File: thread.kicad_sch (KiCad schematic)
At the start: 35 parts, among them J3002 TC2050, J3003 Conn_01x06_Pin, J3004 SMA-KWE901, Q3001 DMG1012T, U3001 nRF52840, X3001 32.768kHz, X3002 25MHz

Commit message: Small fixes
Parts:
- added R3005: 10k, symbol Device:R
- R3003: value 100k -> 10k
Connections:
- net VDD_nRF: now also R3005.1
- net nRF_SPI0_CS0: now also R3005.2
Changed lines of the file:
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@@
 	)
 	(junction
+		(at 217.17 142.24)
+		(diameter 0)
+		(color 0 0 0 0)
+	)
+	(junction
 		(at 80.01 153.67)
 		(diameter 0)
@@
 	(wire
 		(pts
-			(xy 193.04 147.32) (xy 210.82 147.32)
-		)
-		(stroke
-			(width 0)
-			(type default)
-		)
-	)
-	(wire
-		(pts
 			(xy 316.23 113.03) (xy 316.23 115.57)
 		)
@@
 	(wire
 		(pts
+			(xy 204.47 149.86) (xy 222.25 149.86)
+		)
+		(stroke
+			(width 0)
+			(type default)
+		)
+	)
+	(wire
+		(pts
 			(xy 283.21 119.38) (xy 283.21 120.65)
 		)
@@
 	(wire
 		(pts
+			(xy 217.17 140.97) (xy 217.17 142.24)
+		)
+		(stroke
+			(width 0)
+			(type default)
+		)
+	)
+	(wire
+		(pts
 			(xy 69.85 161.29) (xy 69.85 163.83)
 		)
@@
 	(wire
 		(pts
+			(xy 217.17 132.08) (xy 217.17 133.35)
+		)
+		(stroke
+			(width 0)
+			(type default)
+		)
+	)
+	(wire
+		(pts
 			(xy 201.93 74.93) (xy 201.93 77.47)
 		)
@@
 	(wire
 		(pts
+			(xy 193.04 147.32) (xy 222.25 147.32)
+		)
+		(stroke
+			(width 0)
+			(type default)
+		)
+	)
+	(wire
+		(pts
 			(xy 229.87 220.98) (xy 250.19 220.98)
 		)
@@
 	(wire
 		(pts
-			(xy 193.04 142.24) (xy 210.82 142.24)
+			(xy 193.04 142.24) (xy 217.17 142.24)
 		)
 		(stroke
@@
 	(wire
 		(pts
+			(xy 217.17 142.24) (xy 222.25 142.24)
+		)
+		(stroke
+			(width 0)
+			(type default)
+		)
+	)
+	(wire
+		(pts
 			(xy 229.87 218.44) (xy 250.19 218.44)
 		)
@@
 	(wire
 		(pts
-			(xy 193.04 144.78) (xy 210.82 144.78)
-		)
-		(stroke
-			(width 0)
-			(type default)
-		)
-	)
-	(wire
-		(pts
 			(xy 64.77 219.71) (xy 73.66 219.71)
 		)
@@
 	(wire
 		(pts
-			(xy 193.04 132.08) (xy 213.36 132.08)
+			(xy 193.04 144.78) (xy 222.25 144.78)
 		)
 		(stroke
@@
 	(wire
 		(pts
-			(xy 210.82 149.86) (xy 204.47 149.86)
+			(xy 193.04 132.08) (xy 213.36 132.08)
 		)
 		(stroke
@@
 	(global_label "nRF_SPI0_CLK"
 		(shape input)
-		(at 210.82 144.78 0)
+		(at 222.25 144.78 0)
 		(fields_autoplaced yes)
 		(effects
@@
 		)
 		(property "Intersheetrefs" "${INTERSHEET_REFS}"
-			(at 227.1099 144.78 0)
+			(at 238.5399 144.78 0)
 			(effects
 				(font
@@
 	(global_label "nRF_SPI0_MOSI"
 		(shape input)
-		(at 210.82 147.32 0)
+		(at 222.25 147.32 0)
 		(fields_autoplaced yes)
 		(effects
@@
 		)
 		(property "Intersheetrefs" "${INTERSHEET_REFS}"
-			(at 228.138 147.32 0)
+			(at 239.568 147.32 0)
 			(effects
 				(font
@@
 	(global_label "nRF_SPI0_CS0"
 		(shape input)
-		(at 210.82 142.24 0)
+		(at 222.25 142.24 0)
 		(fields_autoplaced yes)
 		(effects
@@
 		)
 		(property "Intersheetrefs" "${INTERSHEET_REFS}"
-			(at 227.2308 142.24 0)
+			(at 238.6608 142.24 0)
 			(effects
 				(font
@@
 	(global_label "nRF_SPI0_MISO"
 		(shape input)
-		(at 210.82 149.86 0)
+		(at 222.25 149.86 0)
 		(fields_autoplaced yes)
 		(effects
@@
 		)
 		(property "Intersheetrefs" "${INTERSHEET_REFS}"
-			(at 228.138 149.86 0)
+			(at 239.568 149.86 0)
 			(effects
 				(font
@@
 			)
 		)
-		(property "Value" "100k"
+		(property "Value" "10k"
 			(at 208.28 191.7699 0)
 			(effects
@@
 	)
 	(symbol
+		(lib_id "Device:R")
+		(at 217.17 137.16 0)
+		(unit 1)
+		(exclude_from_sim no)
+		(in_bom yes)
+		(on_board yes)
+		(dnp no)
+		(property "Reference" "R3005"
+			(at 218.948 133.858 0)
+			(effects
+				(font
+					(size 1.27 1.27)
+				)
+				(justify left)
+			)
+		)
+		(property "Value" "10k"
+			(at 218.948 136.398 0)
+			(effects
+				(font
+					(size 1.27 1.27)
+				)
+				(justify left)
+			)
+		)
+		(property "Footprint" ""
+			(at 215.392 137.16 90)
+			(effects
+				(font
+					(size 1.27 1.27)
+				)
+				(hide yes)
+			)
+		)
+		(property "Datasheet" "~"
+			(at 217.17 137.16 0)
+			(effects
+				(font
+					(size 1.27 1.27)
+				)
+				(hide yes)
+			)
+		)
+		(property "Description" "Resistor"
+			(at 217.17 137.16 0)
+			(effects
+				(font
+					(size 1.27 1.27)
+				)
+				(hide yes)
+			)
+		)
+		(pin "2"
+		)
+		(pin "1"
+		)
+		(instances
+			(project ""
+				(path "/b43b7bca-e50d-42ec-8ff0-e0016dfefe0a/ab846a80-6f2e-4d25-9090-1f6af1d6fbdd"
+					(reference "R3005")
+					(unit 1)
+				)
+			)
+		)
+	)
+	(symbol
 		(lib_id "power:GND")
 		(at 226.06 135.89 0)
@@
 					(unit 1)
 				)
+			)
+		)
+	)
+	(symbol
+		(lib_id "power:VDD")
+		(at 217.17 132.08 0)
+		(unit 1)
+		(exclude_from_sim no)
+		(in_bom yes)
+		(on_board yes)
+		(dnp no)
+		(property "Reference" "#PWR03030"
+			(at 217.17 135.89 0)
+			(effects
+				(font
+					(size 1.27 1.27)
+				)
+				(hide yes)
+			)
+		)
+		(property "Value" "VDD_nRF"
+			(at 219.202 127.762 0)
+			(effects
+				(font
+					(size 1.27 1.27)
+				)
+			)
+		)
+		(property "Footprint" ""
+			(at 217.17 132.08 0)
+			(effects
+				(font
+					(size 1.27 1.27)
+				)
+				(hide yes)
+			)
+		)
+		(property "Datasheet" ""
+			(at 217.17 132.08 0)
+			(effects
+				(font
+					(size 1.27 1.27)
+				)
+				(hide yes)
+			)
+		)
+		(property "Description" "Power symbol creates a global label with name \"VDD\""
+			(at 217.17 132.08 0)
+			(effects
+				(font
+					(size 1.27 1.27)
+				)
+				(hide yes)
+			)
+		)
+		(pin "1"
+		)
+		(instances
+			(project "Leonhart"
+				(path "/b43b7bca-e50d-42ec-8ff0-e0016dfefe0a/ab846a80-6f2e-4d25-9090-1f6af1d6fbdd"
+					(reference "#PWR03030")
+					(unit 1)
+				)

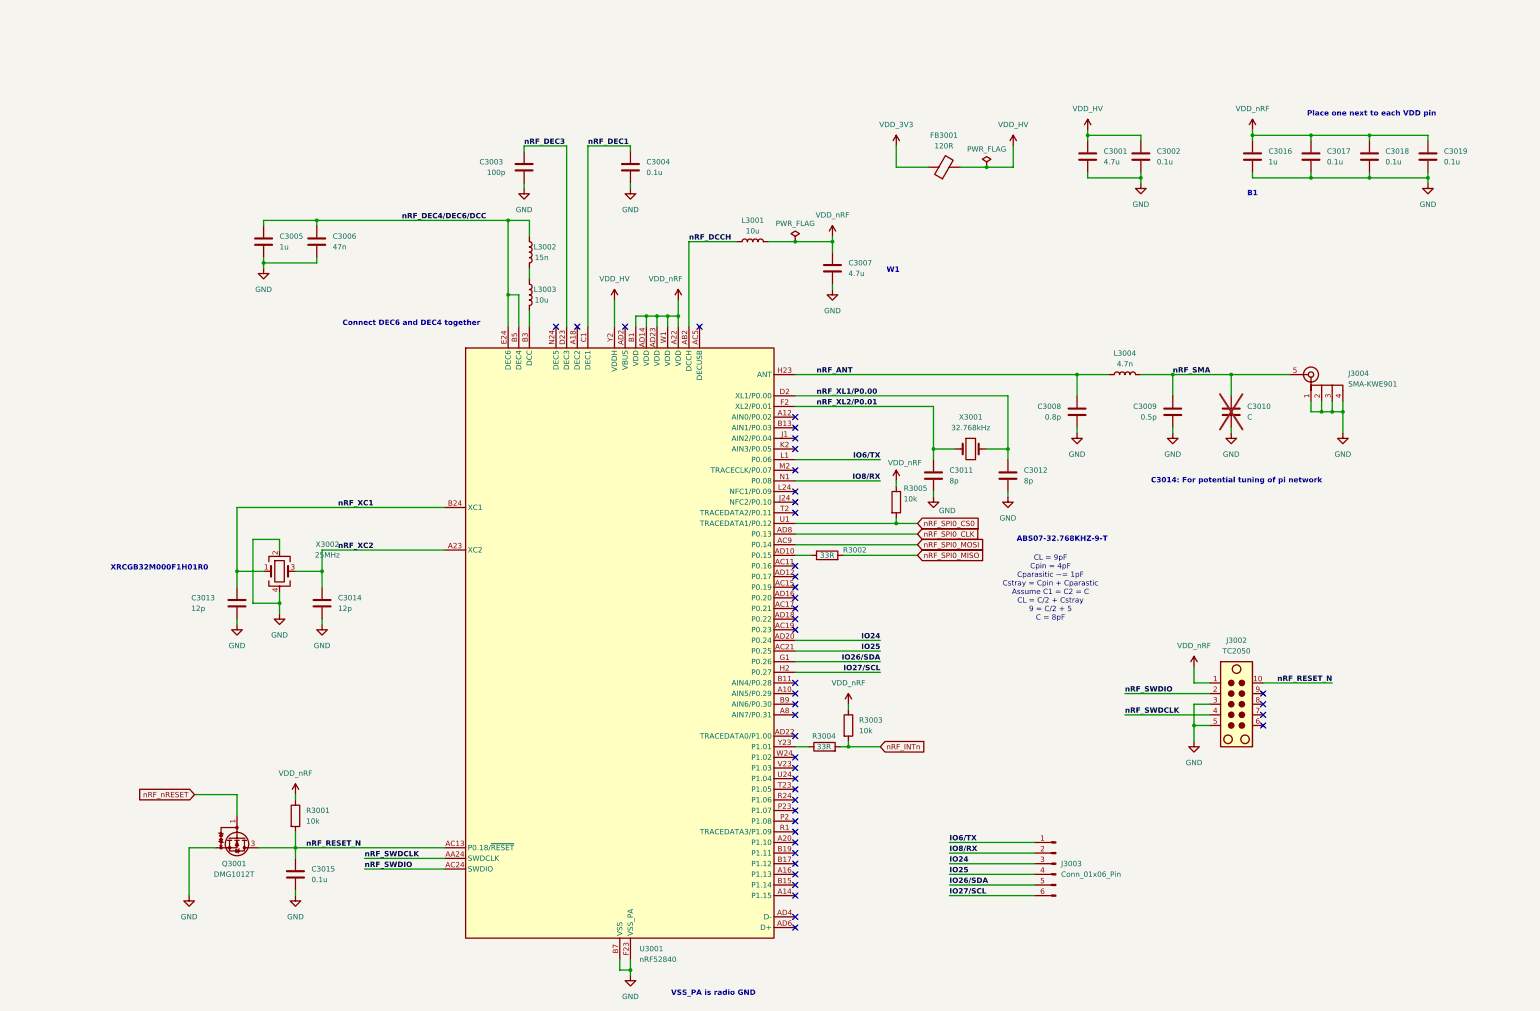
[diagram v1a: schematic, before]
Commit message: More SoC fanout
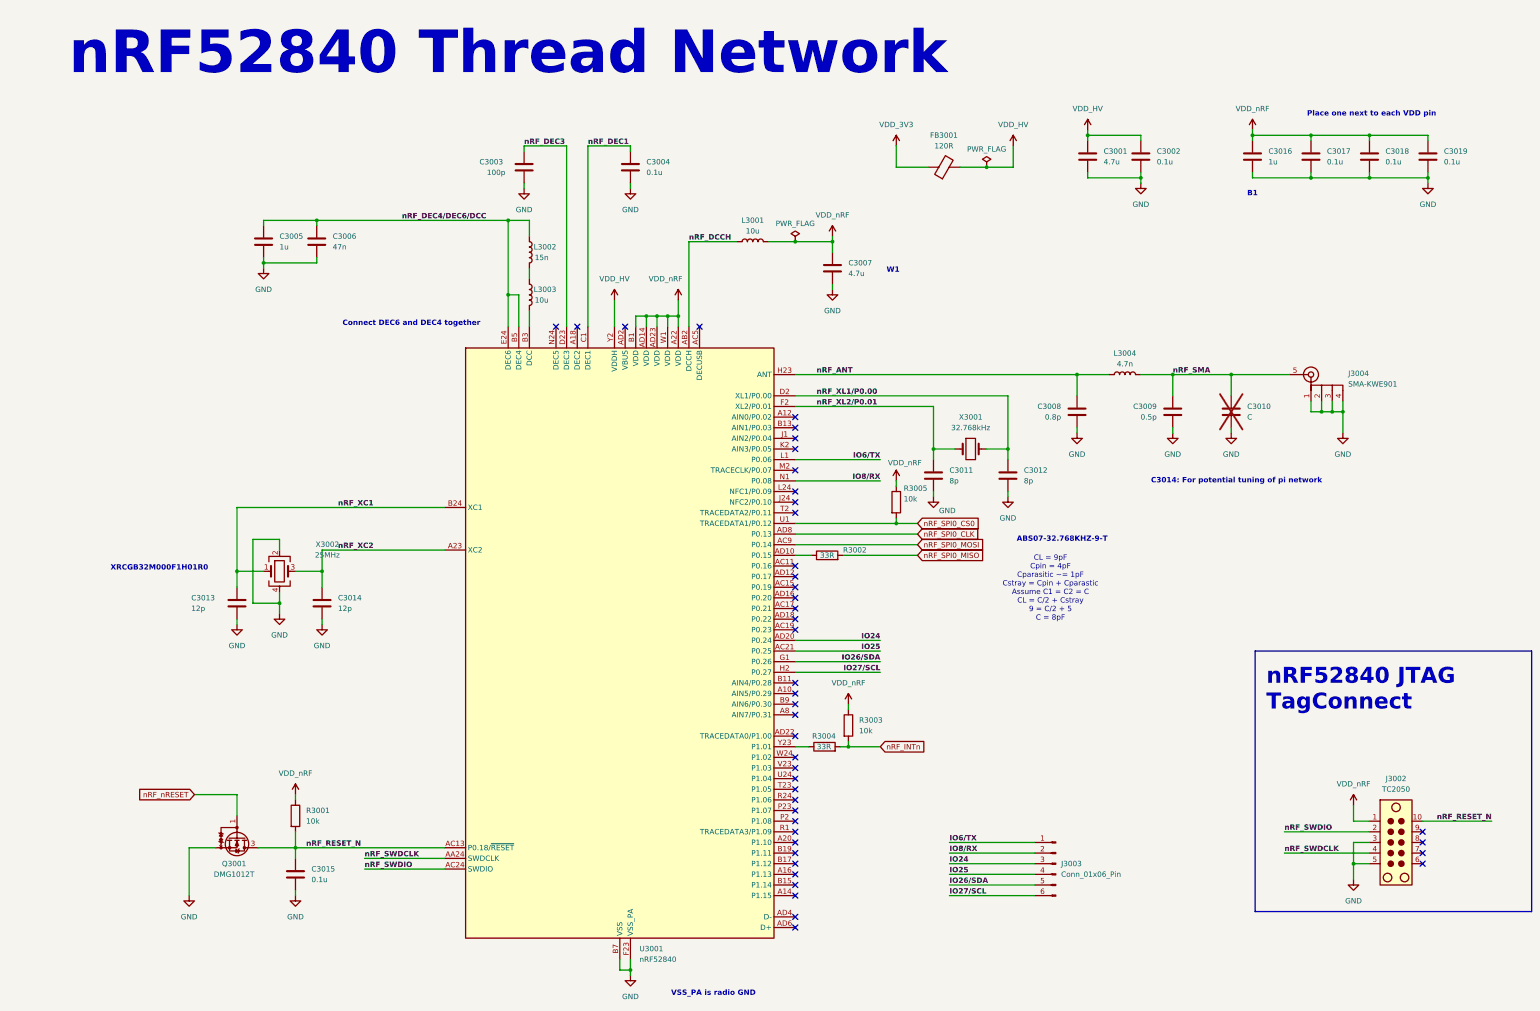
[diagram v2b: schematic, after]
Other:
- note added: "nRF52840 JTAG TagConnect"
- note added: "nRF52840 Thread Network"
- moved on the sheet: J3002
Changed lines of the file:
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@@
 	(generator_version "9.0")
 	(paper "A3")
+	(rectangle
+		(start 302.895 172.72)
+		(end 368.935 234.95)
+		(stroke
+			(width 0)
+			(type default)
+		)
+		(fill
+			(type none)
+		)
+	)
 	(text "W1"
 		(exclude_from_sim no)
@@
 		)
 	)
+	(text "nRF52840 Thread Network"
+		(exclude_from_sim no)
+		(at 124.46 29.972 0)
+		(effects
+			(font
+				(size 10.16 10.16)
+				(thickness 2.54)
+				(bold yes)
+			)
+		)
+	)
 	(text "C3014: For potential tuning of pi network"
 		(exclude_from_sim no)
@@
 		)
 	)
+	(text "nRF52840 JTAG\nTagConnect"
+		(exclude_from_sim no)
+		(at 305.562 181.864 0)
+		(effects
+			(font
+				(size 3.81 3.81)
+				(thickness 1.016)
+				(bold yes)
+			)
+			(justify left)
+		)
+	)
 	(text "B1"
 		(exclude_from_sim no)
@@
 	)
 	(junction
-		(at 288.29 190.5)
+		(at 326.39 223.52)
 		(diameter 0)
 		(color 0 0 0 0)
@@
 	)
 	(no_connect
-		(at 304.8 185.42)
+		(at 342.9 218.44)
 	)
 	(no_connect
@@
 	)
 	(no_connect
-		(at 304.8 190.5)
+		(at 342.9 223.52)
 	)
 	(no_connect
@@
 	)
 	(no_connect
-		(at 304.8 187.96)
+		(at 342.9 220.98)
 	)
 	(no_connect
@@
 	)
 	(no_connect
-		(at 304.8 182.88)
+		(at 342.9 215.9)
 	)
 	(no_connect
@@
 	(wire
 		(pts
-			(xy 292.1 185.42) (xy 288.29 185.42)
+			(xy 330.2 218.44) (xy 326.39 218.44)
 		)
 		(stroke
@@
 	(wire
 		(pts
-			(xy 288.29 190.5) (xy 288.29 194.31)
+			(xy 326.39 223.52) (xy 326.39 227.33)
 		)
 		(stroke
@@
 	(wire
 		(pts
-			(xy 288.29 180.34) (xy 292.1 180.34)
+			(xy 326.39 213.36) (xy 330.2 213.36)
 		)
 		(stroke
@@
 	(wire
 		(pts
-			(xy 288.29 176.53) (xy 288.29 180.34)
+			(xy 326.39 209.55) (xy 326.39 213.36)
 		)
 		(stroke
@@
 	(wire
 		(pts
-			(xy 271.78 182.88) (xy 292.1 182.88)
+			(xy 309.88 215.9) (xy 330.2 215.9)
 		)
 		(stroke
@@
 	(wire
 		(pts
-			(xy 288.29 190.5) (xy 292.1 190.5)
+			(xy 326.39 223.52) (xy 330.2 223.52)
 		)
 		(stroke
@@
 	(wire
 		(pts
-			(xy 304.8 180.34) (xy 321.31 180.34)
+			(xy 342.9 213.36) (xy 359.41 213.36)
 		)
 		(stroke
@@
 	(wire
 		(pts
-			(xy 288.29 185.42) (xy 288.29 190.5)
+			(xy 326.39 218.44) (xy 326.39 223.52)
 		)
 		(stroke
@@
 	(wire
 		(pts
-			(xy 271.78 187.96) (xy 292.1 187.96)
+			(xy 309.88 220.98) (xy 330.2 220.98)
 		)
 		(stroke
@@
 	)
 	(label "nRF_SWDIO"
-		(at 271.78 182.88 0)
+		(at 309.88 215.9 0)
 		(effects
 			(font
@@
 	)
 	(label "nRF_SWDCLK"
-		(at 271.78 187.96 0)
+		(at 309.88 220.98 0)
 		(effects
 			(font
@@
 	)
 	(label "nRF_RESET_N"
-		(at 321.31 180.34 180)
+		(at 359.41 213.36 180)
 		(effects
 			(font
@@
 	(symbol
 		(lib_id "Connector:TC2050")
-		(at 297.18 185.42 0)
+		(at 335.28 218.44 0)
 		(unit 1)
 		(exclude_from_sim no)
@@
 		(fields_autoplaced yes)
 		(property "Reference" "J3002"
-			(at 298.45 170.18 0)
+			(at 336.55 203.2 0)
 			(effects
 				(font
@@
 		)
 		(property "Value" "TC2050"
-			(at 298.45 172.72 0)
+			(at 336.55 205.74 0)
 			(effects
 				(font
@@
 		)
 		(property "Footprint" "Connector:Tag-Connect_TC2050-IDC-NL_2x05_P1.27mm_Vertical"
-			(at 298.45 185.42 0)
+			(at 336.55 218.44 0)
 			(effects
 				(font
@@
 		)
 		(property "Datasheet" "https://www.tag-connect.com/wp-content/uploads/bsk-pdf-manager/TC2050-IDC-NL_Datasheet_8.pdf"
-			(at 298.45 185.42 0)
+			(at 336.55 218.44 0)
 			(effects
 				(font
@@
 		)
 		(property "Description" "Tag-Connect’s 10-pins connector"
-			(at 297.18 185.42 0)
+			(at 335.28 218.44 0)
 			(effects
 				(font
@@
 	(symbol
 		(lib_id "power:VDD")
-		(at 288.29 176.53 0)
+		(at 326.39 209.55 0)
 		(unit 1)
 		(exclude_from_sim no)
@@
 		(fields_autoplaced yes)
 		(property "Reference" "#PWR03020"
-			(at 288.29 180.34 0)
+			(at 326.39 213.36 0)
 			(effects
 				(font
@@
 		)
 		(property "Value" "VDD_nRF"
-			(at 288.29 171.45 0)
+			(at 326.39 204.47 0)
 			(effects
 				(font
@@
 		)
 		(property "Footprint" ""
-			(at 288.29 176.53 0)
+			(at 326.39 209.55 0)
 			(effects
 				(font
@@
 		)
 		(property "Datasheet" ""
-			(at 288.29 176.53 0)
+			(at 326.39 209.55 0)
 			(effects
 				(font
@@
 		)
 		(property "Description" "Power symbol creates a global label with name \"VDD\""
-			(at 288.29 176.53 0)
+			(at 326.39 209.55 0)
 			(effects
 				(font
@@
 	(symbol
 		(lib_id "power:GND")
-		(at 288.29 194.31 0)
+		(at 326.39 227.33 0)
 		(unit 1)
 		(exclude_from_sim no)
@@
 		(fields_autoplaced yes)
 		(property "Reference" "#PWR03021"
-			(at 288.29 200.66 0)
+			(at 326.39 233.68 0)
 			(effects
 				(font
@@
 		)
 		(property "Value" "GND"
-			(at 288.29 199.39 0)
+			(at 326.39 232.41 0)
 			(effects
 				(font
@@
 		)
 		(property "Footprint" ""
-			(at 288.29 194.31 0)
+			(at 326.39 227.33 0)
 			(effects
 				(font
@@
 		)
 		(property "Datasheet" ""
-			(at 288.29 194.31 0)
+			(at 326.39 227.33 0)
 			(effects
 				(font
@@
 		)
 		(property "Description" "Power symbol creates a global label with name \"GND\" , ground"
-			(at 288.29 194.31 0)
+			(at 326.39 227.33 0)
 			(effects
 				(font

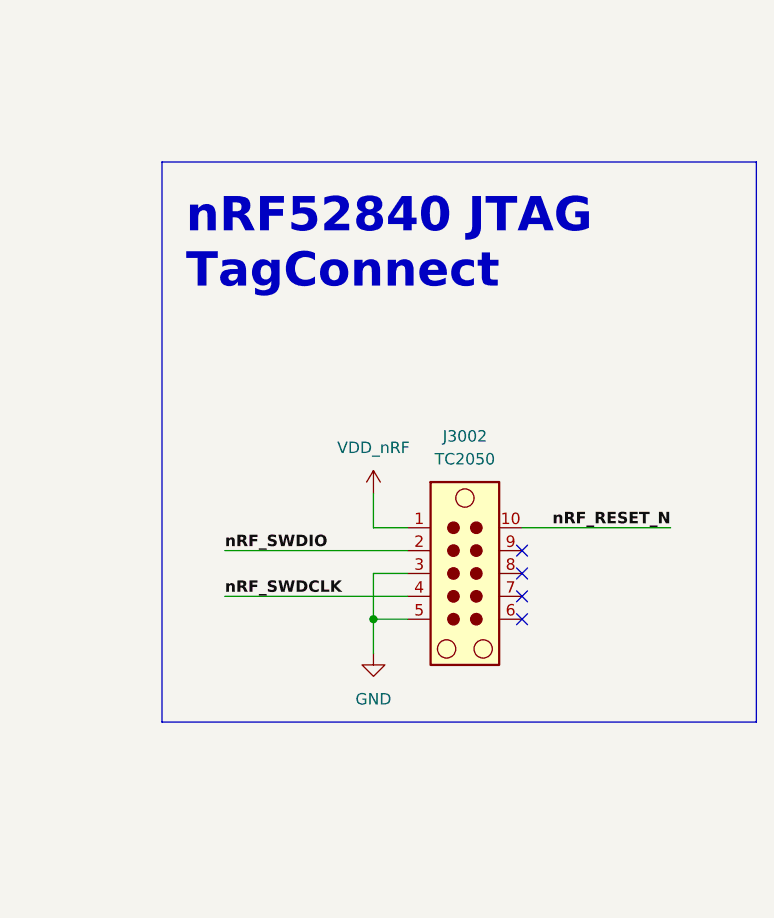
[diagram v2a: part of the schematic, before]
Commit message: Restarted SoC power decoupling based on manufacturer capabilities
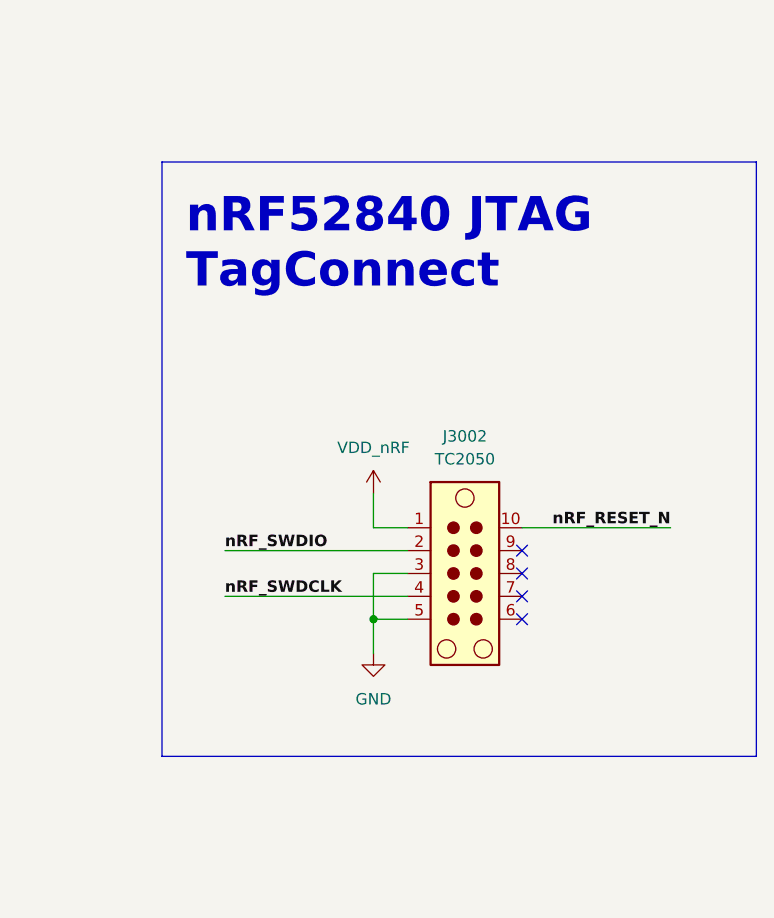
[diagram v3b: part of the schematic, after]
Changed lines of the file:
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@@
 	(rectangle
 		(start 302.895 172.72)
-		(end 368.935 234.95)
+		(end 368.935 238.76)
 		(stroke
 			(width 0)

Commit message: Started USB and OSC routing
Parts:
- X3002: value 25MHz -> 32MHz
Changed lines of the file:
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@@
 		(on_board yes)
 		(dnp no)
-		(fields_autoplaced yes)
 		(property "Reference" "X3002"
-			(at 81.28 147.2498 0)
+			(at 75.438 145.542 0)
 			(effects
 				(font
@@
 			)
 		)
-		(property "Value" "25MHz"
-			(at 81.28 149.7898 0)
+		(property "Value" "32MHz"
+			(at 75.438 148.082 0)
 			(effects
 				(font
